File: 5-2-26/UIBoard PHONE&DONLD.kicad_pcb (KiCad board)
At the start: 2 copper layers, 285.5 x 122.3 mm, 128 parts, among them J3 430450200, J4 430450200, J5 M22-7130442, J7 22035035, Q1 2N3904, Q2 2N3904, Q3 2N3904, Q4 2N3904, SW1 A8L-11-12N1, U1 UA78M05-Q1, U2 MCP2562-E-P, U3 CD4511BPWR, U4 UA78M05-Q1, U5 7 Segment Display, U6 STM32 Nucleo F446RE, U7 PCF8574AP

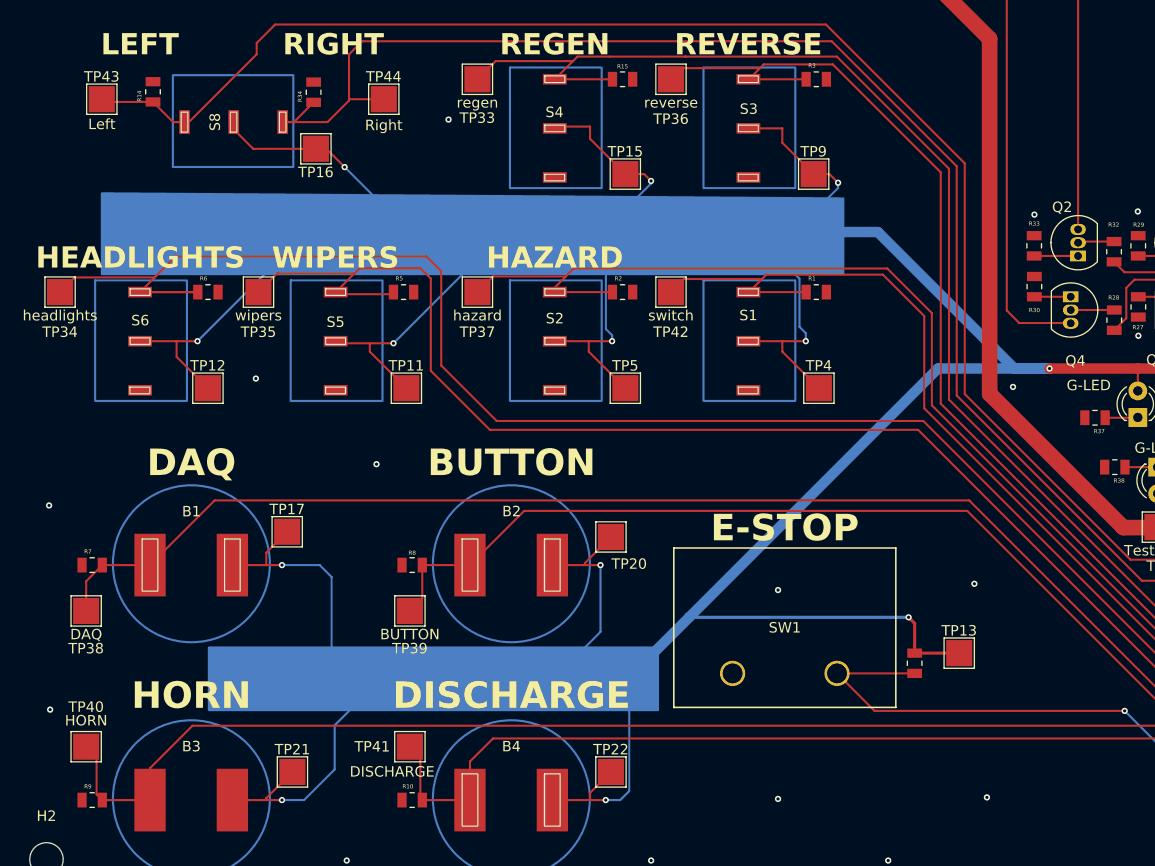
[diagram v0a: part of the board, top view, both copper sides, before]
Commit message: added a few more vias
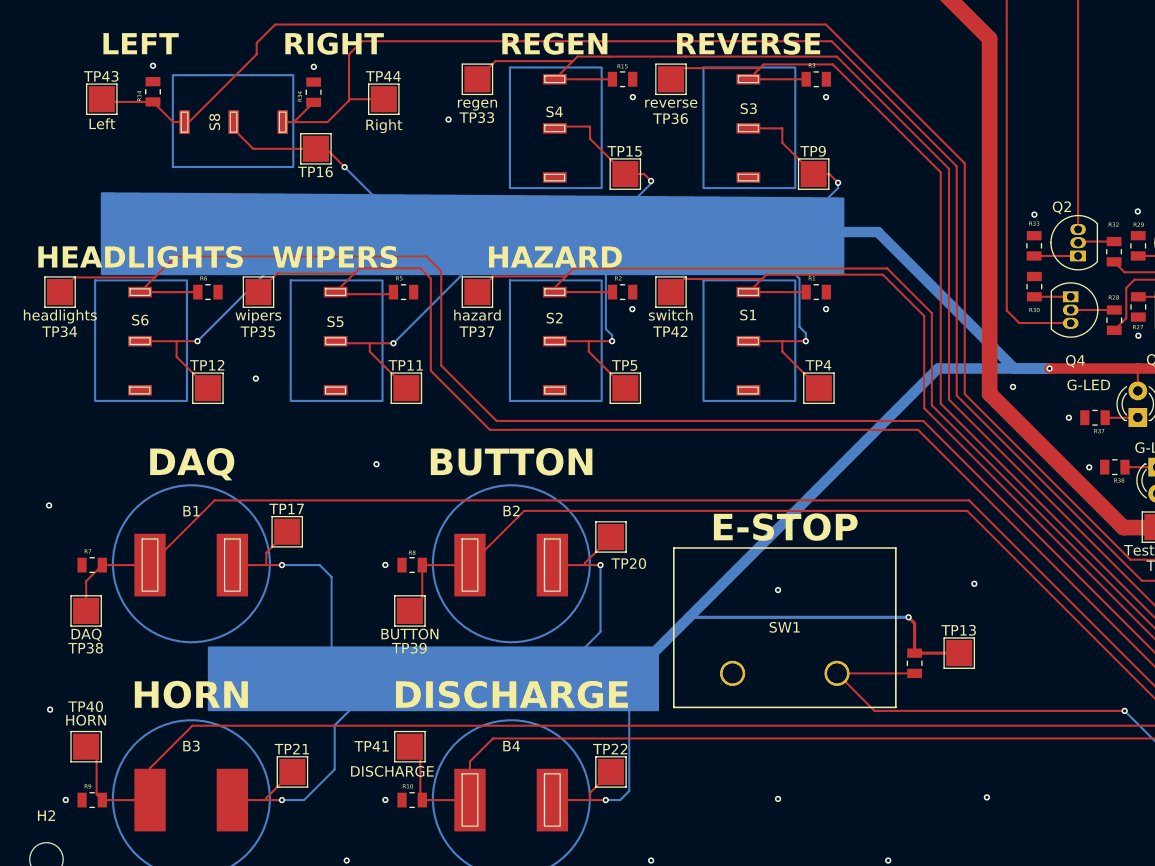
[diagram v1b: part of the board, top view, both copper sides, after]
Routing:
- net GND: vias 66 -> 77
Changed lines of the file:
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@@
 	)
 	(via
+		(at 565.85 55.8)
+		(size 0.6)
+		(drill 0.3)
+		(layers "F.Cu" "B.Cu")
+		(free yes)
+		(net "GND")
+	)
+	(via
 		(at 679.5 122.25)
 		(size 0.6)
@@
 	)
 	(via
+		(at 584.35 55.8)
+		(size 0.6)
+		(drill 0.3)
+		(layers "F.Cu" "B.Cu")
+		(free yes)
+		(net "GND")
+	)
+	(via
 		(at 687.2 128.9)
 		(size 0.6)
@@
 	)
 	(via
+		(at 565.8 76.1)
+		(size 0.6)
+		(drill 0.3)
+		(layers "F.Cu" "B.Cu")
+		(free yes)
+		(net "GND")
+	)
+	(via
 		(at 714.849403 67.997681)
 		(size 0.6)
@@
 	)
 	(via
+		(at 519.9 52.8)
+		(size 0.6)
+		(drill 0.3)
+		(layers "F.Cu" "B.Cu")
+		(free yes)
+		(net "GND")
+	)
+	(via
 		(at 785.55 53.5)
 		(size 0.6)
@@
 	)
 	(via
+		(at 542.15 123.1)
+		(size 0.6)
+		(drill 0.3)
+		(layers "F.Cu" "B.Cu")
+		(free yes)
+		(net "GND")
+	)
+	(via
 		(at 744.7 82.25)
 		(size 0.6)
@@
 	)
 	(via
+		(at 542.15 100.6)
+		(size 0.6)
+		(drill 0.3)
+		(layers "F.Cu" "B.Cu")
+		(free yes)
+		(net "GND")
+	)
+	(via
+		(at 584.35 76.1)
+		(size 0.6)
+		(drill 0.3)
+		(layers "F.Cu" "B.Cu")
+		(free yes)
+		(net "GND")
+	)
+	(via
 		(at 729.5 22.5)
 		(size 0.6)
@@
 	)
 	(via
+		(at 511.55 123.1)
+		(size 0.6)
+		(drill 0.3)
+		(layers "F.Cu" "B.Cu")
+		(free yes)
+		(net "GND")
+	)
+	(via
 		(at 548.2 57.95)
 		(size 0.6)
@@
 	)
 	(via
+		(at 535.3 52.9)
+		(size 0.6)
+		(drill 0.3)
+		(layers "F.Cu" "B.Cu")
+		(free yes)
+		(net "GND")
+	)
+	(via
 		(at 590.3 128.9)
 		(size 0.6)
@@
 	)
 	(via
+		(at 609.55 91.25)
+		(size 0.6)
+		(drill 0.3)
+		(layers "F.Cu" "B.Cu")
+		(free yes)
+		(net "GND")
+	)
+	(via
+		(at 607.6 86.5)
+		(size 0.6)
+		(drill 0.3)
+		(layers "F.Cu" "B.Cu")
+		(free yes)
+		(net "GND")
+	)
+	(via
 		(at 768.2 128.9)
 		(size 0.6)
@@
 	)
 	(segment
+		(start 612.97 91.23)
+		(end 616.1 91.23)
+		(width 0.2)
+		(layer "F.Cu")
+		(net "Net-(D4-K)")
+	)
+	(segment
 		(start 604.275 71.01)
 		(end 608.48 71.01)
@@
 		(net "Net-(D3-K)")
 	)
-	(segment
-		(start 612.97 91.23)
-		(end 616.1 91.23)
-		(width 0.2)
-		(layer "F.Cu")
-		(net "Net-(D4-K)")
-	)
 	(zone

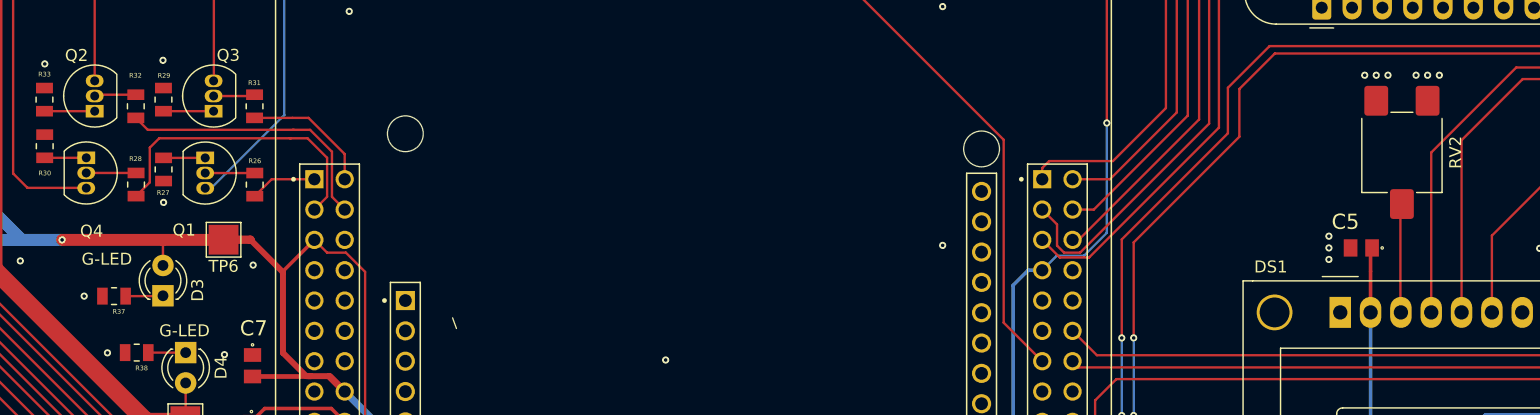
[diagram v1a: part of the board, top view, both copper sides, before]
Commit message: changed 20k potentometer footprint
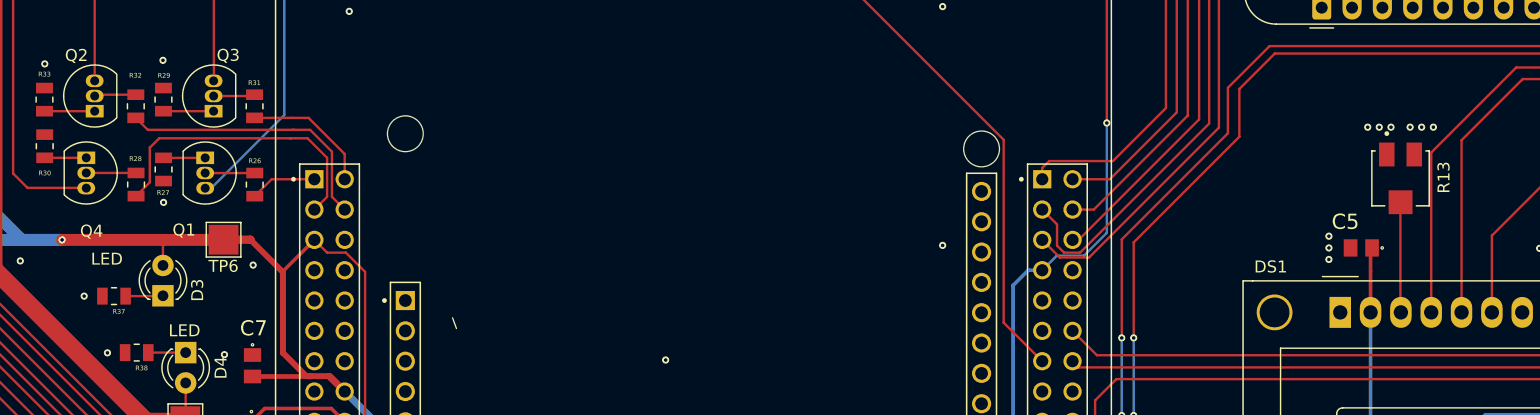
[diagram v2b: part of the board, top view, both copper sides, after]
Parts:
- removed RV2: 20kOhms, Potentiometer_SMD:Potentiometer_ACP_CA6-VSMD_Vertical
- added R13: 3214J-1-203E, SMV_ICs:TRIM_3214J-1-203E, F.Cu at (717.9, 76.6)
- D3, D4: value G-LED -> LED
